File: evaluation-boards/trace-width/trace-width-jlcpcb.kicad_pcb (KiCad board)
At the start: 4 copper layers, 80 x 130 mm, 26 parts, among them J1 CONN_COAXIAL, J10 CONN_COAXIAL, J11 CONN_COAXIAL, J12 CONN_COAXIAL, J2 CONN_COAXIAL, J3 CONN_COAXIAL, J4 CONN_COAXIAL, J5 CONN_COAXIAL, J6 CONN_COAXIAL, J7 CONN_COAXIAL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

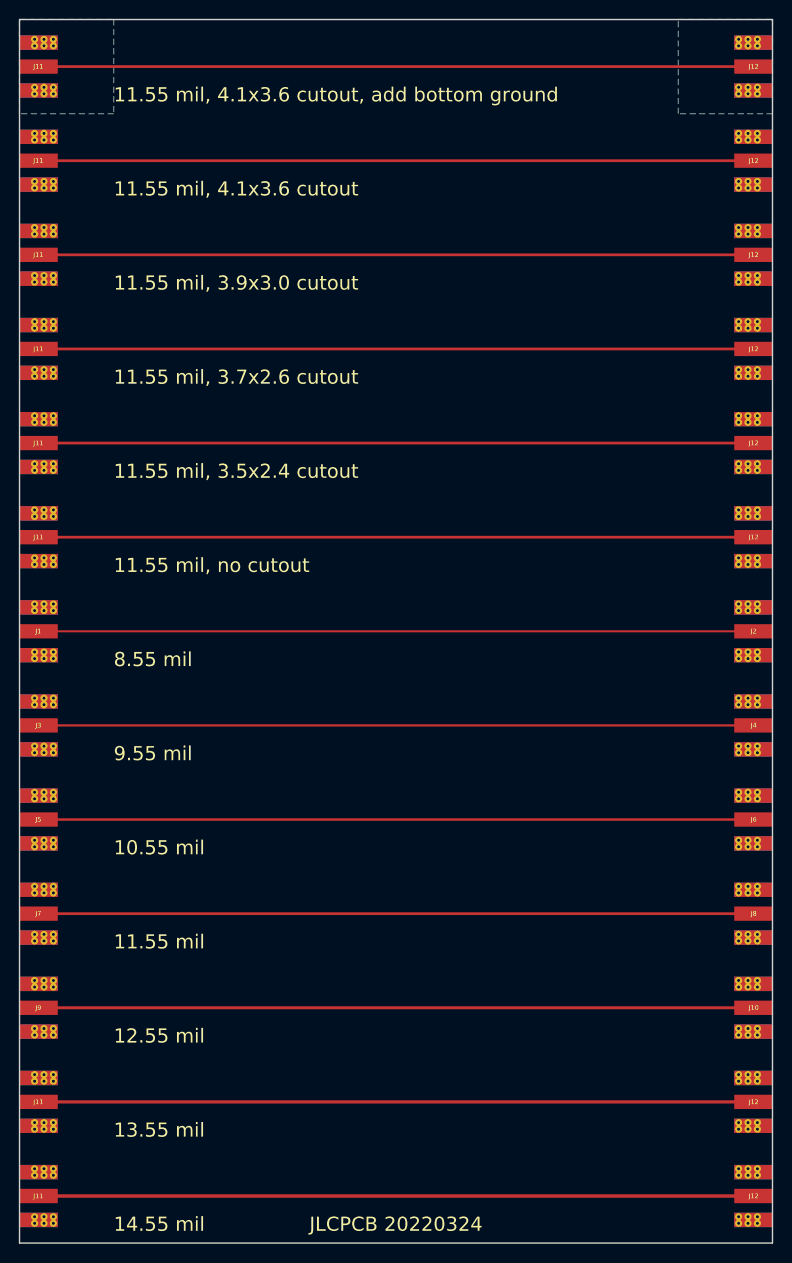
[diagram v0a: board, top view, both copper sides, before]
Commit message: Update JLCPCB 7628 stack-up trace width board
JLCPCB changed their stack-ups at some point in 2022. This board is
intended to confirm the appropriate trace width for 50 ohm microstrip on
their new 6-layer stack-up.
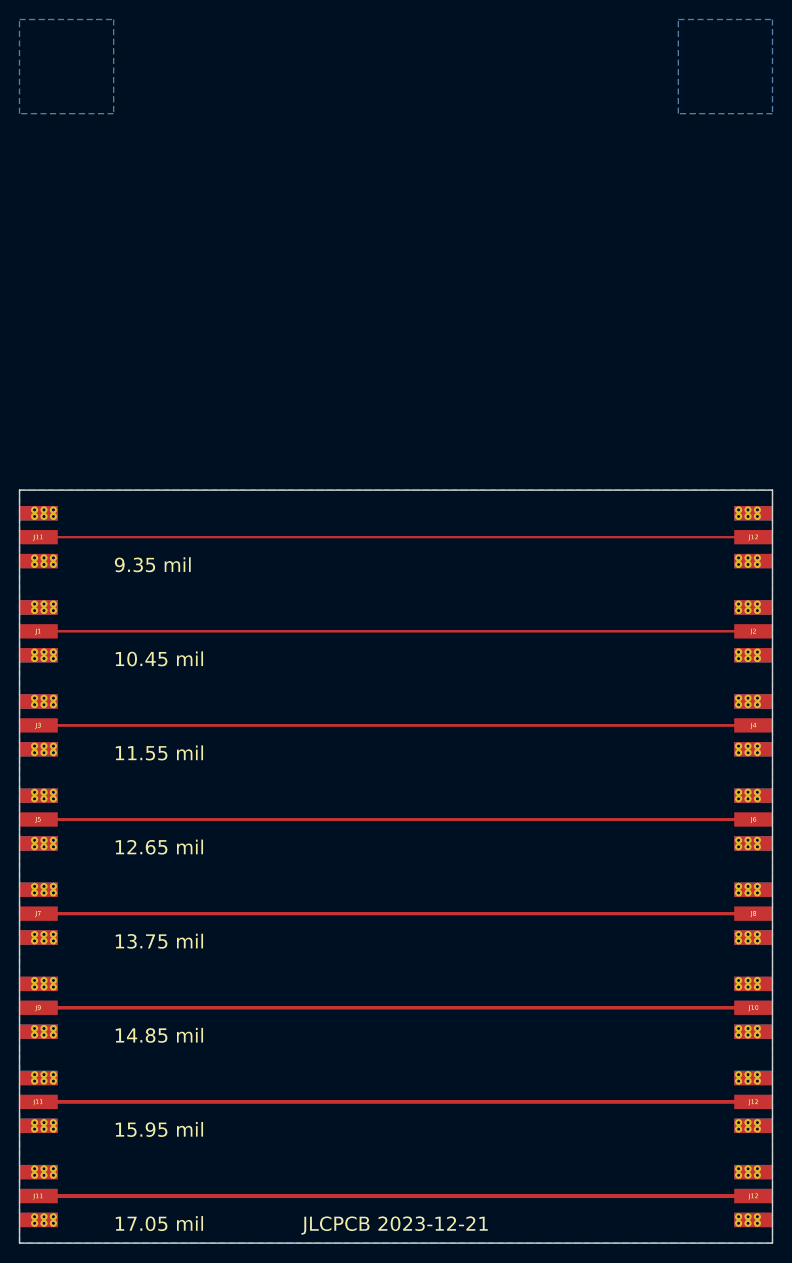
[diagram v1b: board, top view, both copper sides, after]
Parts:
- removed the J11 at (120.0, 20.0)
- removed the J11 at (120.0, 30.0)
- removed the J11 at (120.0, 40.0)
- removed the J11 at (120.0, 50.0)
- removed the J11 at (120.0, 60.0)
- removed the J12 at (200.0, 20.0)
- removed the J12 at (200.0, 30.0)
- removed the J12 at (200.0, 40.0)
- removed the J12 at (200.0, 50.0)
- removed the J12 at (200.0, 60.0)
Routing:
- net Net-(J11-Pad1): track 606.5 -> 227.4 mm
- added copper zone on In1.Cu, net GND
- added copper zone on In2.Cu, net GND
- added copper zone on In3.Cu, net GND
- added copper zone on In4.Cu, net GND
- removed copper zone on C2, net GND
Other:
- board size 80 x 130 mm -> 80 x 80 mm
- copper layers 4 -> 6
- net class Default removed
- board text added: "10.45 mil"
- board text added: "12.65 mil"
- board text added: "13.75 mil"
- board text added: "14.85 mil"
- board text added: "15.95 mil"
- board text added: "17.05 mil"
- board text added: "9.35 mil"
- board text added: "JLCPCB 2023-12-21"
- board text removed: "10.55 mil"
- board text removed: "11.55 mil, 3.5x2.4 cutout"
- board text removed: "11.55 mil, 3.7x2.6 cutout"
- board text removed: "11.55 mil, 3.9x3.0 cutout"
- board text removed: "11.55 mil, 4.1x3.6 cutout"
- board text removed: "11.55 mil, 4.1x3.6 cutout, add bottom ground"
- board text removed: "11.55 mil, no cutout"
- board text removed: "12.55 mil"
- board text removed: "13.55 mil"
- board text removed: "14.55 mil"
- board text removed: "8.55 mil"
- board text removed: "9.55 mil"
- board text removed: "JLCPCB 20220324"

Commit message: Update trace width and SMA connector boards
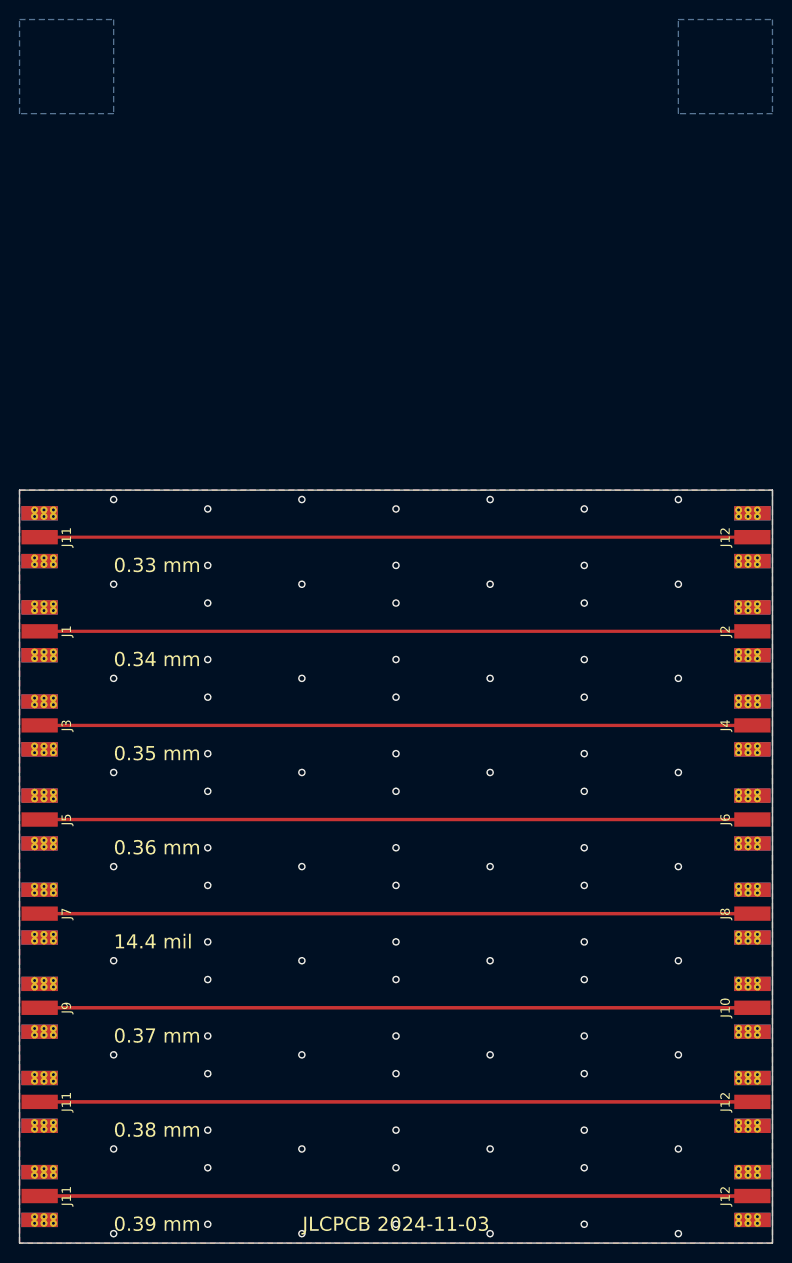
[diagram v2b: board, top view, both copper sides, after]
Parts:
- J1, J10, J11 (x3), J12 (x3), J2, J3, J4, J5, J6, J7, J8, J9: footprint gsg-modules:SMA-EDGE -> sma-variants:Linx_SMA_CONSMA003.062
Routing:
- net GND: vias 0 -> 84
- added copper zone on F.Cu, net GND
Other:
- board text added: "0.33 mm"
- board text added: "0.34 mm"
- board text added: "0.35 mm"
- board text added: "0.36 mm"
- board text added: "0.37 mm"
- board text added: "0.38 mm"
- board text added: "0.39 mm"
- board text added: "14.4 mil"
- board text added: "JLCPCB 2024-11-03"
- board text removed: "10.45 mil"
- board text removed: "11.55 mil"
- board text removed: "12.65 mil"
- board text removed: "13.75 mil"
- board text removed: "14.85 mil"
- board text removed: "15.95 mil"
- board text removed: "17.05 mil"
- board text removed: "9.35 mil"
- board text removed: "JLCPCB 2023-12-21"
